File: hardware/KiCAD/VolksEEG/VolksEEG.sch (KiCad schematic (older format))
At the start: 1 part, among them U7 ISO7761DW

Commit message: re-organised the root schematic, plumbed in the power and signal lines. renamed the nrf52840 sheet to highlight the fact it is the Feather Sense Express board.
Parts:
- removed U7: ISO7761DW, Package_SO:SOIC-16W_7.5x10.3mm_P1.27mm, symbol Isolator:ISO7761DW
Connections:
- net labels removed: +3V3, GNDA, GNDD, VDC
- wire segments 26 -> 40
- no-connect marks 2 -> 0

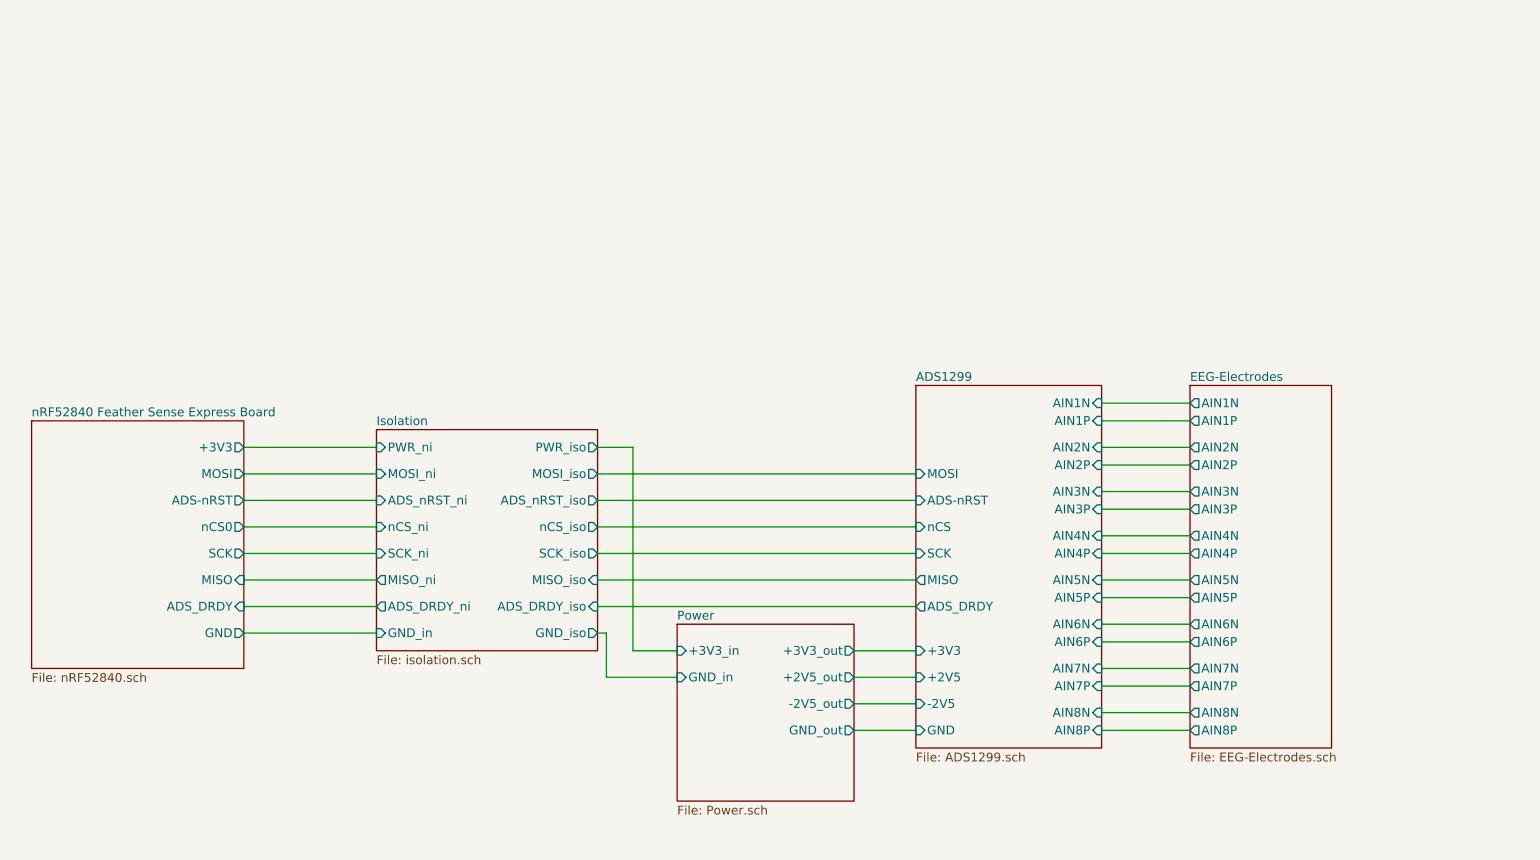
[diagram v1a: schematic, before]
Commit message: Some re-naming and added some pull ups to the nrf schematic.
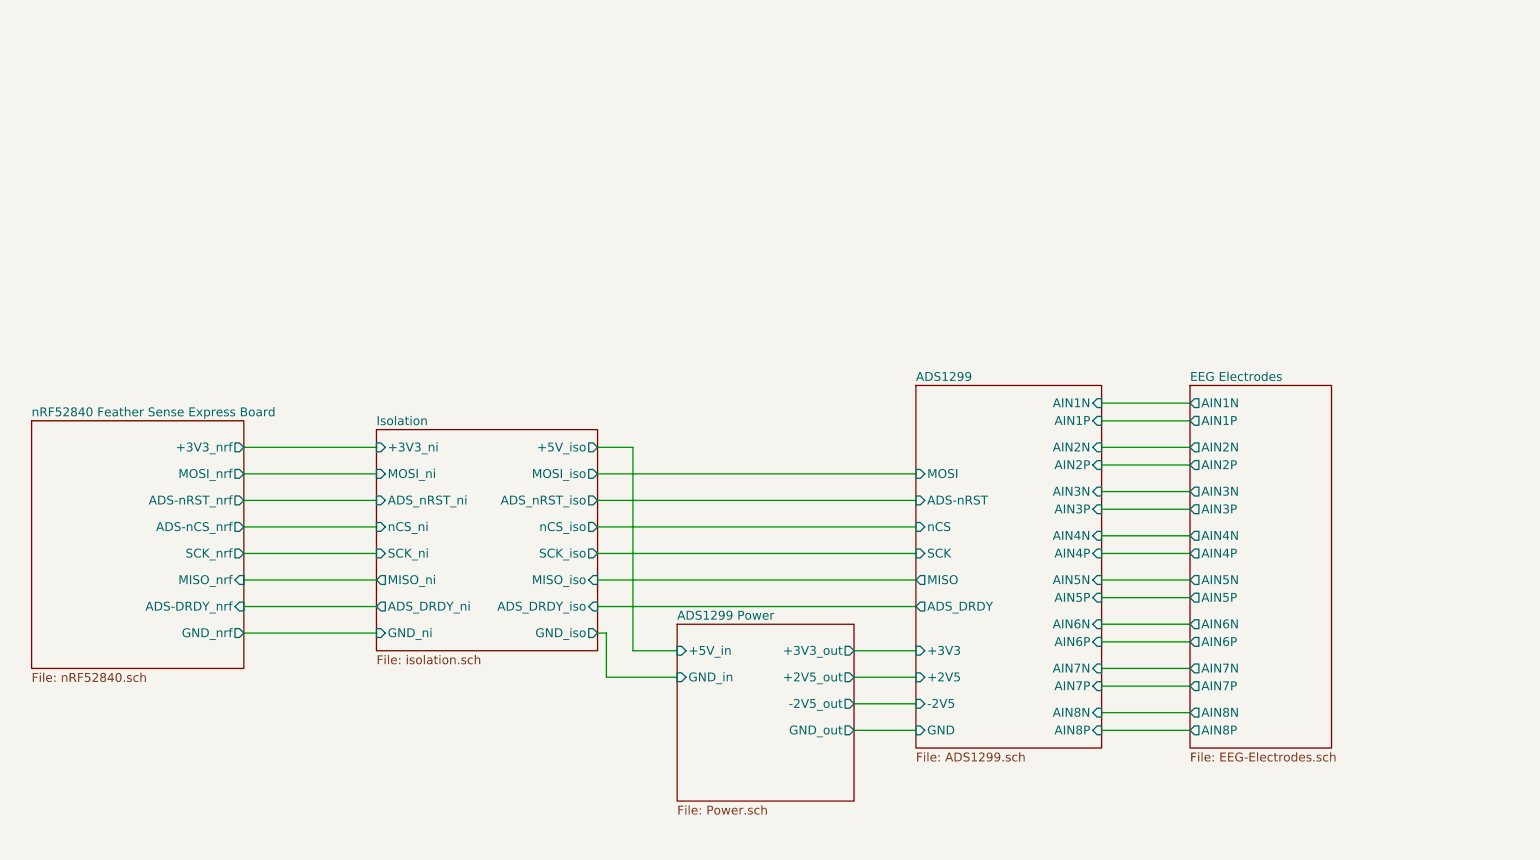
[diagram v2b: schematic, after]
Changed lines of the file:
@@
 S 5250 4350 1000 1000
 U 615BA255
-F0 "Power" 50
+F0 "ADS1299 Power" 50
 F1 "Power.sch" 50
-F2 "+3V3_in" I L 5250 4500 50
+F2 "+5V_in" I L 5250 4500 50
 F3 "GND_in" I L 5250 4650 50
 F4 "+3V3_out" O R 6250 4500 50
@@
 F0 "nRF52840 Feather Sense Express Board" 50
 F1 "nRF52840.sch" 50
-F2 "MOSI" O R 2800 3500 50
-F3 "SCK" O R 2800 3950 50
-F4 "MISO" I R 2800 4100 50
-F5 "ADS-nRST" O R 2800 3650 50
-F6 "nCS0" O R 2800 3800 50
-F7 "ADS_DRDY" I R 2800 4250 50
-F8 "+3V3" O R 2800 3350 50
-F9 "GND" O R 2800 4400 50
+F2 "MOSI_nrf" O R 2800 3500 50
+F3 "SCK_nrf" O R 2800 3950 50
+F4 "MISO_nrf" I R 2800 4100 50
+F5 "ADS-nRST_nrf" O R 2800 3650 50
+F6 "ADS-nCS_nrf" O R 2800 3800 50
+F7 "ADS-DRDY_nrf" I R 2800 4250 50
+F8 "+3V3_nrf" O R 2800 3350 50
+F9 "GND_nrf" O R 2800 4400 50
 $EndSheet
 $Sheet
@@
 F0 "Isolation" 50
 F1 "isolation.sch" 50
-F2 "PWR_ni" I L 3550 3350 50
-F3 "GND_in" I L 3550 4400 50
-F4 "PWR_iso" O R 4800 3350 50
+F2 "+3V3_ni" I L 3550 3350 50
+F3 "GND_ni" I L 3550 4400 50
+F4 "+5V_iso" O R 4800 3350 50
 F5 "GND_iso" O R 4800 4400 50
 F6 "MOSI_iso" O R 4800 3500 50
@@
 S 8150 3000 800  2050
 U 615BA18D
-F0 "EEG-Electrodes" 50
+F0 "EEG Electrodes" 50
 F1 "EEG-Electrodes.sch" 50
 F2 "AIN2N" O L 8150 3350 50

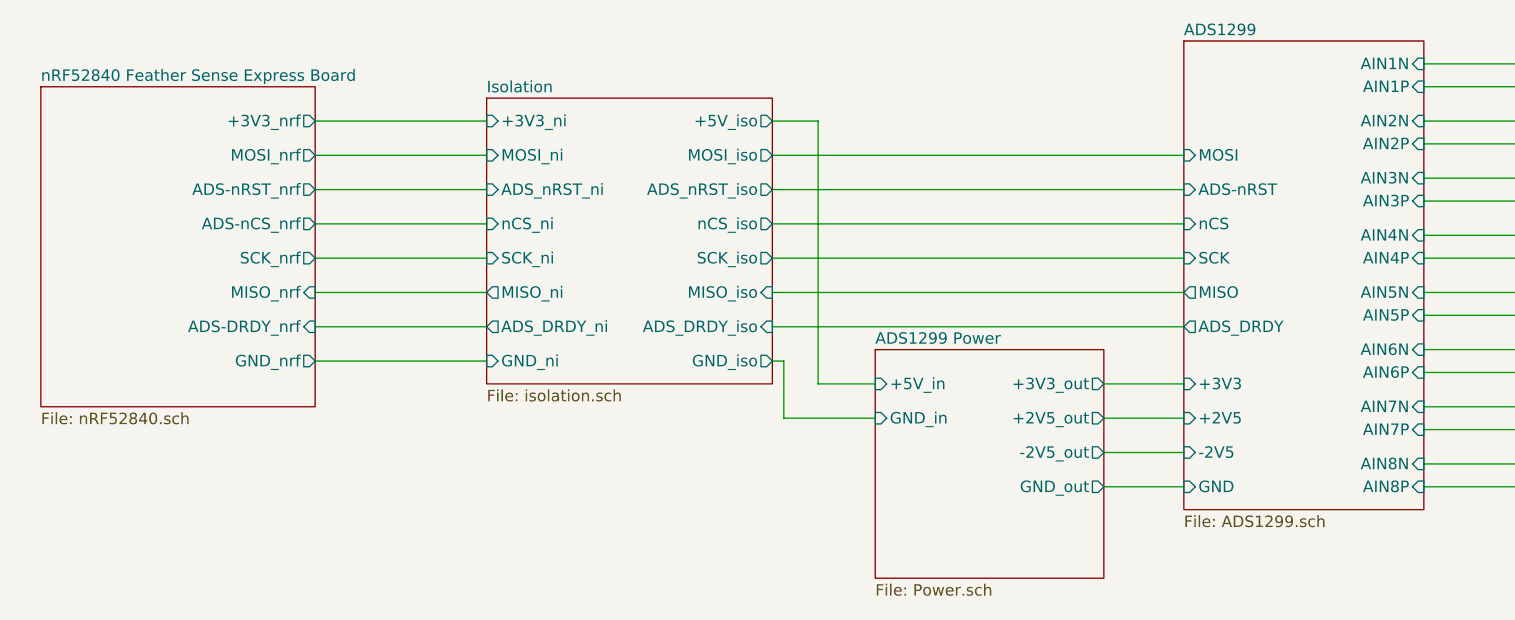
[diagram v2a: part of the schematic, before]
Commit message: Added Digi-key's kicad component libraries, some work done on power, think this will change but capturing it here for posterity.
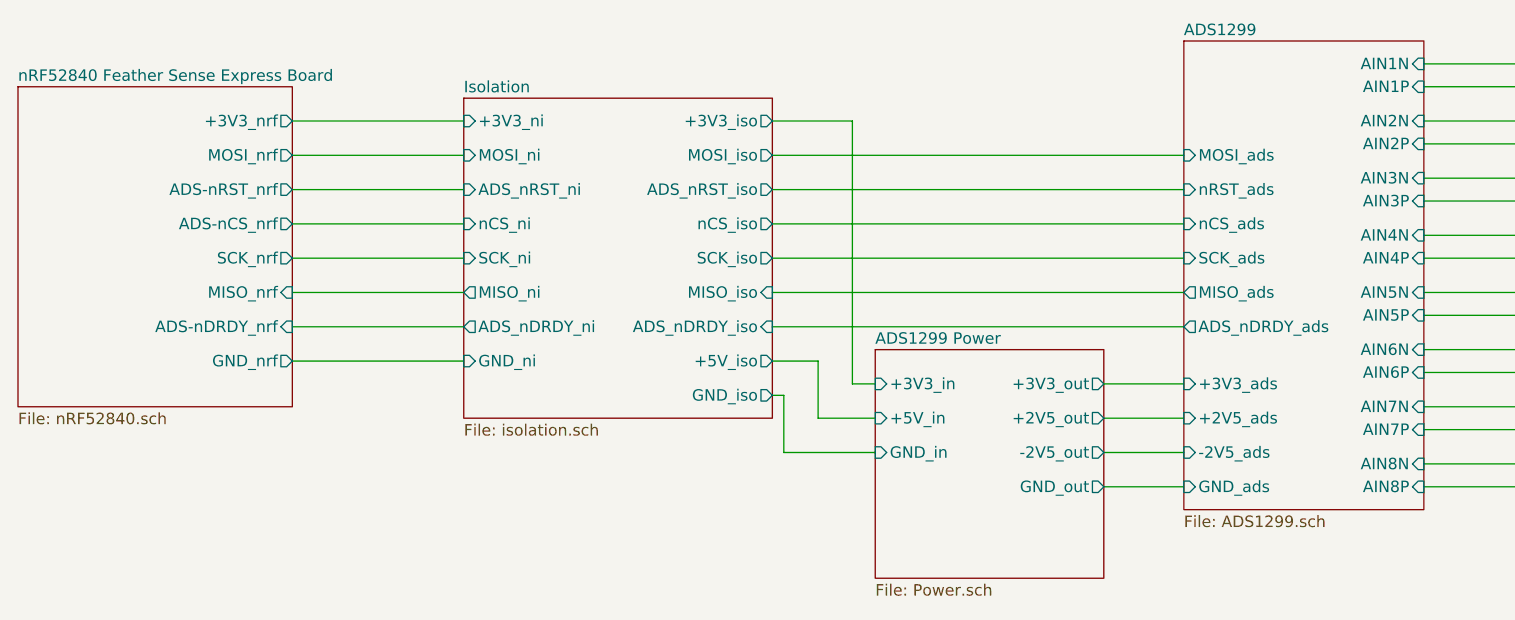
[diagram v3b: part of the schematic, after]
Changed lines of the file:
@@
 F0 "ADS1299" 50
 F1 "ADS1299.sch" 50
-F2 "nCS" I L 6600 3800 50
-F3 "SCK" I L 6600 3950 50
-F4 "MOSI" I L 6600 3500 50
-F5 "MISO" O L 6600 4100 50
-F6 "ADS-nRST" I L 6600 3650 50
+F2 "nCS_ads" I L 6600 3800 50
+F3 "SCK_ads" I L 6600 3950 50
+F4 "MOSI_ads" I L 6600 3500 50
+F5 "MISO_ads" O L 6600 4100 50
+F6 "nRST_ads" I L 6600 3650 50
 F7 "AIN5N" I R 7650 4100 50
 F8 "AIN5P" I R 7650 4200 50
@@
 F21 "AIN4N" I R 7650 3850 50
 F22 "AIN4P" I R 7650 3950 50
-F23 "ADS_DRDY" O L 6600 4250 50
-F24 "+3V3" I L 6600 4500 50
-F25 "+2V5" I L 6600 4650 50
-F26 "-2V5" I L 6600 4800 50
-F27 "GND" I L 6600 4950 50
+F23 "ADS_nDRDY_ads" O L 6600 4250 50
+F24 "+3V3_ads" I L 6600 4500 50
+F25 "+2V5_ads" I L 6600 4650 50
+F26 "-2V5_ads" I L 6600 4800 50
+F27 "GND_ads" I L 6600 4950 50
 $EndSheet
 $Sheet
@@
 F0 "ADS1299 Power" 50
 F1 "Power.sch" 50
-F2 "+5V_in" I L 5250 4500 50
-F3 "GND_in" I L 5250 4650 50
+F2 "+3V3_in" I L 5250 4500 50
+F3 "GND_in" I L 5250 4800 50
 F4 "+3V3_out" O R 6250 4500 50
 F5 "+2V5_out" O R 6250 4650 50
 F6 "-2V5_out" O R 6250 4800 50
 F7 "GND_out" O R 6250 4950 50
+F8 "+5V_in" I L 5250 4650 50
 $EndSheet
 $Sheet
-S 1600 3200 1200 1400
+S 1500 3200 1200 1400
 U 615BA20B
 F0 "nRF52840 Feather Sense Express Board" 50
 F1 "nRF52840.sch" 50
-F2 "MOSI_nrf" O R 2800 3500 50
-F3 "SCK_nrf" O R 2800 3950 50
-F4 "MISO_nrf" I R 2800 4100 50
-F5 "ADS-nRST_nrf" O R 2800 3650 50
-F6 "ADS-nCS_nrf" O R 2800 3800 50
-F7 "ADS-DRDY_nrf" I R 2800 4250 50
-F8 "+3V3_nrf" O R 2800 3350 50
-F9 "GND_nrf" O R 2800 4400 50
-$EndSheet
-$Sheet
-S 3550 3250 1250 1250
-U 61731DC5
-F0 "Isolation" 50
-F1 "isolation.sch" 50
-F2 "+3V3_ni" I L 3550 3350 50
-F3 "GND_ni" I L 3550 4400 50
-F4 "+5V_iso" O R 4800 3350 50
-F5 "GND_iso" O R 4800 4400 50
-F6 "MOSI_iso" O R 4800 3500 50
-F7 "ADS_nRST_iso" O R 4800 3650 50
-F8 "nCS_iso" O R 4800 3800 50
-F9 "SCK_iso" O R 4800 3950 50
-F10 "MISO_iso" I R 4800 4100 50
-F11 "ADS_DRDY_iso" I R 4800 4250 50
-F12 "MOSI_ni" I L 3550 3500 50
-F13 "ADS_nRST_ni" I L 3550 3650 50
-F14 "nCS_ni" I L 3550 3800 50
-F15 "SCK_ni" I L 3550 3950 50
-F16 "MISO_ni" O L 3550 4100 50
-F17 "ADS_DRDY_ni" O L 3550 4250 50
+F2 "MOSI_nrf" O R 2700 3500 50
+F3 "SCK_nrf" O R 2700 3950 50
+F4 "MISO_nrf" I R 2700 4100 50
+F5 "ADS-nRST_nrf" O R 2700 3650 50
+F6 "ADS-nCS_nrf" O R 2700 3800 50
+F7 "ADS-nDRDY_nrf" I R 2700 4250 50
+F8 "+3V3_nrf" O R 2700 3350 50
+F9 "GND_nrf" O R 2700 4400 50
 $EndSheet
 Wire Wire Line
-	2800 3500 3550 3500
+	2700 3500 3450 3500
 Wire Wire Line
-	3550 3650 2800 3650
+	3450 3650 2700 3650
 Wire Wire Line
-	2800 3800 3550 3800
+	2700 3800 3450 3800
 Wire Wire Line
-	3550 3950 2800 3950
+	3450 3950 2700 3950
 Wire Wire Line
-	2800 4100 3550 4100
+	2700 4100 3450 4100
 $Sheet
 S 8150 3000 800  2050
@@
 	6600 4250 4800 4250
 Wire Wire Line
-	4800 3350 5000 3350
+	4800 3350 5150 3350
 Wire Wire Line
-	5000 3350 5000 4500
+	5150 3350 5150 4500
 Wire Wire Line
-	4800 4400 4850 4400
+	4800 4550 4850 4550
 Wire Wire Line
-	4850 4400 4850 4650
+	4850 4550 4850 4800
 Wire Wire Line
-	4850 4650 5250 4650
+	4850 4800 5250 4800
 Wire Wire Line
-	5000 4500 5250 4500
+	5150 4500 5250 4500
 Wire Wire Line
 	6250 4500 6600 4500
@@
 	6600 4950 6250 4950
 Wire Wire Line
-	2800 4250 3550 4250
+	2700 4250 3450 4250
 Wire Wire Line
-	2800 3350 3550 3350
+	2700 3350 3450 3350
 Wire Wire Line
-	2800 4400 3550 4400
+	2700 4400 3450 4400
+$Sheet
+S 3450 3250 1350 1400
+U 61731DC5
+F0 "Isolation" 50
+F1 "isolation.sch" 50
+F2 "+3V3_ni" I L 3450 3350 50
+F3 "GND_ni" I L 3450 4400 50
+F4 "+3V3_iso" O R 4800 3350 50
+F5 "GND_iso" O R 4800 4550 50
+F6 "MOSI_iso" O R 4800 3500 50
+F7 "ADS_nRST_iso" O R 4800 3650 50
+F8 "nCS_iso" O R 4800 3800 50
+F9 "SCK_iso" O R 4800 3950 50
+F10 "MISO_iso" I R 4800 4100 50
+F11 "ADS_nDRDY_iso" I R 4800 4250 50
+F12 "MOSI_ni" I L 3450 3500 50
+F13 "ADS_nRST_ni" I L 3450 3650 50
+F14 "nCS_ni" I L 3450 3800 50
+F15 "SCK_ni" I L 3450 3950 50
+F16 "MISO_ni" O L 3450 4100 50
+F17 "ADS_nDRDY_ni" O L 3450 4250 50
+F18 "+5V_iso" O R 4800 4400 50
+$EndSheet
+Wire Wire Line
+	4800 4400 5000 4400
+Wire Wire Line
+	5000 4400 5000 4650
+Wire Wire Line
+	5000 4650 5250 4650
 $EndSCHEMATC

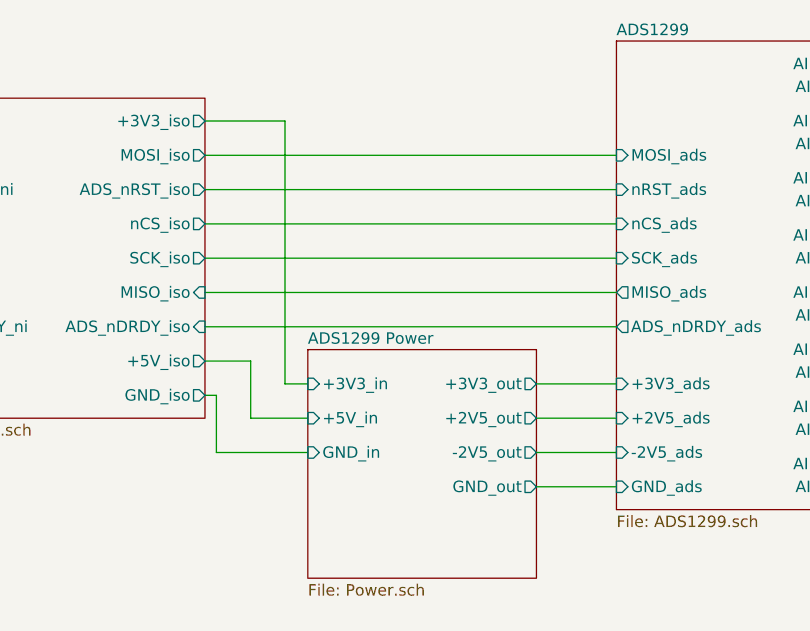
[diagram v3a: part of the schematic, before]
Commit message: Rejigged the power around so that the 3v3 supply is only generated once.
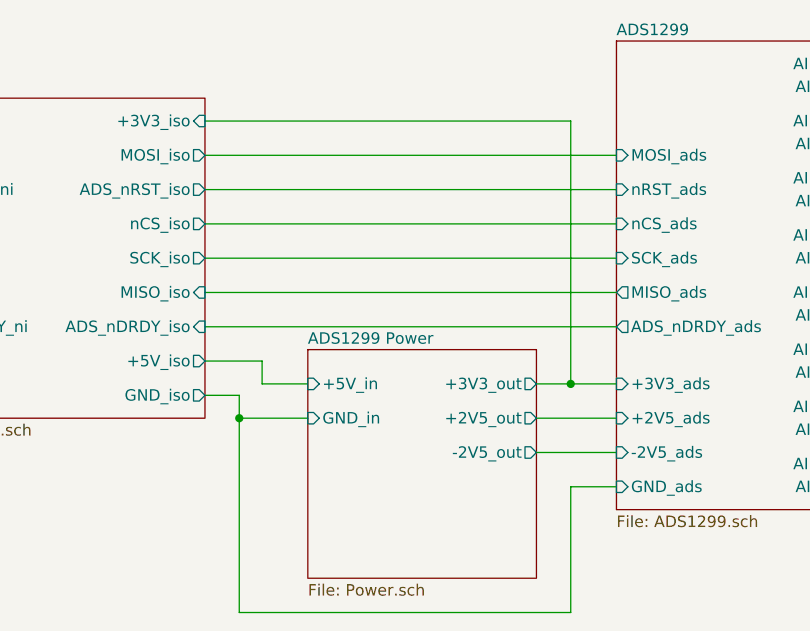
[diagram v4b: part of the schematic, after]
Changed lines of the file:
@@
 F0 "ADS1299 Power" 50
 F1 "Power.sch" 50
-F2 "+3V3_in" I L 5250 4500 50
-F3 "GND_in" I L 5250 4800 50
-F4 "+3V3_out" O R 6250 4500 50
-F5 "+2V5_out" O R 6250 4650 50
-F6 "-2V5_out" O R 6250 4800 50
-F7 "GND_out" O R 6250 4950 50
-F8 "+5V_in" I L 5250 4650 50
+F2 "GND_in" I L 5250 4650 50
+F3 "+3V3_out" O R 6250 4500 50
+F4 "+2V5_out" O R 6250 4650 50
+F5 "-2V5_out" O R 6250 4800 50
+F6 "+5V_in" I L 5250 4500 50
 $EndSheet
 $Sheet
@@
 	6600 4250 4800 4250
 Wire Wire Line
-	4800 3350 5150 3350
+	4800 4550 4950 4550
 Wire Wire Line
-	5150 3350 5150 4500
+	4950 4550 4950 4650
 Wire Wire Line
-	4800 4550 4850 4550
+	4950 4650 5250 4650
 Wire Wire Line
-	4850 4550 4850 4800
-Wire Wire Line
-	4850 4800 5250 4800
-Wire Wire Line
-	5150 4500 5250 4500
-Wire Wire Line
-	6250 4500 6600 4500
+	6250 4500 6400 4500
 Wire Wire Line
 	6600 4650 6250 4650
 Wire Wire Line
 	6250 4800 6600 4800
-Wire Wire Line
-	6600 4950 6250 4950
 Wire Wire Line
 	2700 4250 3450 4250
@@
 F2 "+3V3_ni" I L 3450 3350 50
 F3 "GND_ni" I L 3450 4400 50
-F4 "+3V3_iso" O R 4800 3350 50
+F4 "+3V3_iso" I R 4800 3350 50
 F5 "GND_iso" O R 4800 4550 50
 F6 "MOSI_iso" O R 4800 3500 50
@@
 $EndSheet
 Wire Wire Line
-	4800 4400 5000 4400
+	4800 4400 5050 4400
 Wire Wire Line
-	5000 4400 5000 4650
+	6400 3350 6400 4500
 Wire Wire Line
-	5000 4650 5250 4650
+	4800 3350 6400 3350
+Connection ~ 6400 4500
+Wire Wire Line
+	6400 4500 6600 4500
+Wire Wire Line
+	5050 4400 5050 4500
+Wire Wire Line
+	5050 4500 5250 4500
+Wire Wire Line
+	6600 4950 6400 4950
+Wire Wire Line
+	6400 4950 6400 5500
+Wire Wire Line
+	6400 5500 4950 5500
+Wire Wire Line
+	4950 5500 4950 4650
+Connection ~ 4950 4650
 $EndSCHEMATC
